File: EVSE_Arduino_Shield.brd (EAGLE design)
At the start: 68.6 x 53.3 mm, 45 parts, among them IC1 TLV1805DBVR, IC2 MT3608, IC3 TC1044S_OA, U2 ARDUINOR3-DIMENSION

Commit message: * Fixed missing values of R2, R3, C5, C1, C6, C4
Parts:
- C1, C4, C5, C6: value (none) -> 10u
- R2: value (none) -> 39k
- R3: value (none) -> 2k
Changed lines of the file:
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@@
 <drawing>
 <settings>
-<setting alwaysvectorfont="yes"/>
+<setting alwaysvectorfont="no"/>
 <setting verticaltext="up"/>
 </settings>
@@
 </autorouter>
 <elements>
-<element name="C1" library="rcl" library_urn="urn:adsk.eagle:library:334" package="C0805" package3d_urn="urn:adsk.eagle:package:23617/2" value="" x="26.5" y="25" smashed="yes">
+<element name="C1" library="rcl" library_urn="urn:adsk.eagle:library:334" package="C0805" package3d_urn="urn:adsk.eagle:package:23617/2" value="10u" x="26.5" y="25" smashed="yes">
 <attribute name="NAME" x="26.5" y="23.5" size="1" layer="25" font="vector" ratio="13" align="center"/>
 <attribute name="POPULARITY" value="88" x="41.74" y="3.41" size="1.778" layer="27" display="off"/>
@@
 <attribute name="VALUE" x="37.095" y="23.635" size="1.27" layer="27" rot="R270"/>
 </element>
-<element name="C4" library="rcl" library_urn="urn:adsk.eagle:library:334" package="C0805" package3d_urn="urn:adsk.eagle:package:23617/2" value="" x="30" y="30.5" smashed="yes" rot="R90">
+<element name="C4" library="rcl" library_urn="urn:adsk.eagle:library:334" package="C0805" package3d_urn="urn:adsk.eagle:package:23617/2" value="10u" x="30" y="30.5" smashed="yes" rot="R90">
 <attribute name="NAME" x="30" y="33.5" size="1" layer="25" font="vector" ratio="13" rot="R90" align="center"/>
 <attribute name="POPULARITY" value="88" x="51.59" y="50.82" size="1.778" layer="27" rot="R90" display="off"/>
@@
 <attribute name="VALUE" x="27.2" y="40.6" size="1.27" layer="27" rot="R270"/>
 </element>
-<element name="R2" library="rcl" library_urn="urn:adsk.eagle:library:334" package="R0603" package3d_urn="urn:adsk.eagle:package:23555/3" value="" x="29.5" y="43" smashed="yes" rot="R270">
+<element name="R2" library="rcl" library_urn="urn:adsk.eagle:library:334" package="R0603" package3d_urn="urn:adsk.eagle:package:23555/3" value="39k" x="29.5" y="43" smashed="yes" rot="R270">
 <attribute name="NAME" x="31" y="43" size="1" layer="25" font="vector" ratio="13" rot="R270" align="center"/>
 <attribute name="POPULARITY" value="70" x="29.5" y="43" size="1.27" layer="27" rot="R270" display="off"/>
@@
 <attribute name="VALUE" x="27.595" y="43.635" size="1.27" layer="27" rot="R270"/>
 </element>
-<element name="R3" library="rcl" library_urn="urn:adsk.eagle:library:334" package="R0603" package3d_urn="urn:adsk.eagle:package:23555/3" value="" x="26.5" y="45" smashed="yes">
+<element name="R3" library="rcl" library_urn="urn:adsk.eagle:library:334" package="R0603" package3d_urn="urn:adsk.eagle:package:23555/3" value="2k" x="26.5" y="45" smashed="yes">
 <attribute name="NAME" x="26.5" y="46.5" size="1" layer="25" font="vector" ratio="13" align="center"/>
 <attribute name="POPULARITY" value="70" x="26.5" y="45" size="1.27" layer="27" display="off"/>
@@
 <attribute name="VALUE" x="25.865" y="43.095" size="1.27" layer="27"/>
 </element>
-<element name="C5" library="rcl" library_urn="urn:adsk.eagle:library:334" package="C0805" package3d_urn="urn:adsk.eagle:package:23617/2" value="" x="23.5" y="44" smashed="yes" rot="R90">
+<element name="C5" library="rcl" library_urn="urn:adsk.eagle:library:334" package="C0805" package3d_urn="urn:adsk.eagle:package:23617/2" value="10u" x="23.5" y="44" smashed="yes" rot="R90">
 <attribute name="NAME" x="21.5" y="44" size="1" layer="25" font="vector" ratio="13" rot="R90" align="center"/>
 <attribute name="POPULARITY" value="88" x="23.5" y="44" size="1.27" layer="27" rot="R90" display="off"/>
@@
 <attribute name="VALUE" x="26.04" y="42.73" size="1.27" layer="27" rot="R90"/>
 </element>
-<element name="C6" library="rcl" library_urn="urn:adsk.eagle:library:334" package="C0805" package3d_urn="urn:adsk.eagle:package:23617/2" value="" x="31.5" y="39.5" smashed="yes" rot="R270">
+<element name="C6" library="rcl" library_urn="urn:adsk.eagle:library:334" package="C0805" package3d_urn="urn:adsk.eagle:package:23617/2" value="10u" x="31.5" y="39.5" smashed="yes" rot="R270">
 <attribute name="NAME" x="31.5" y="36" size="1" layer="25" font="vector" ratio="13" rot="R270" align="center"/>
 <attribute name="POPULARITY" value="88" x="31.5" y="39.5" size="1.27" layer="27" rot="R270" display="off"/>

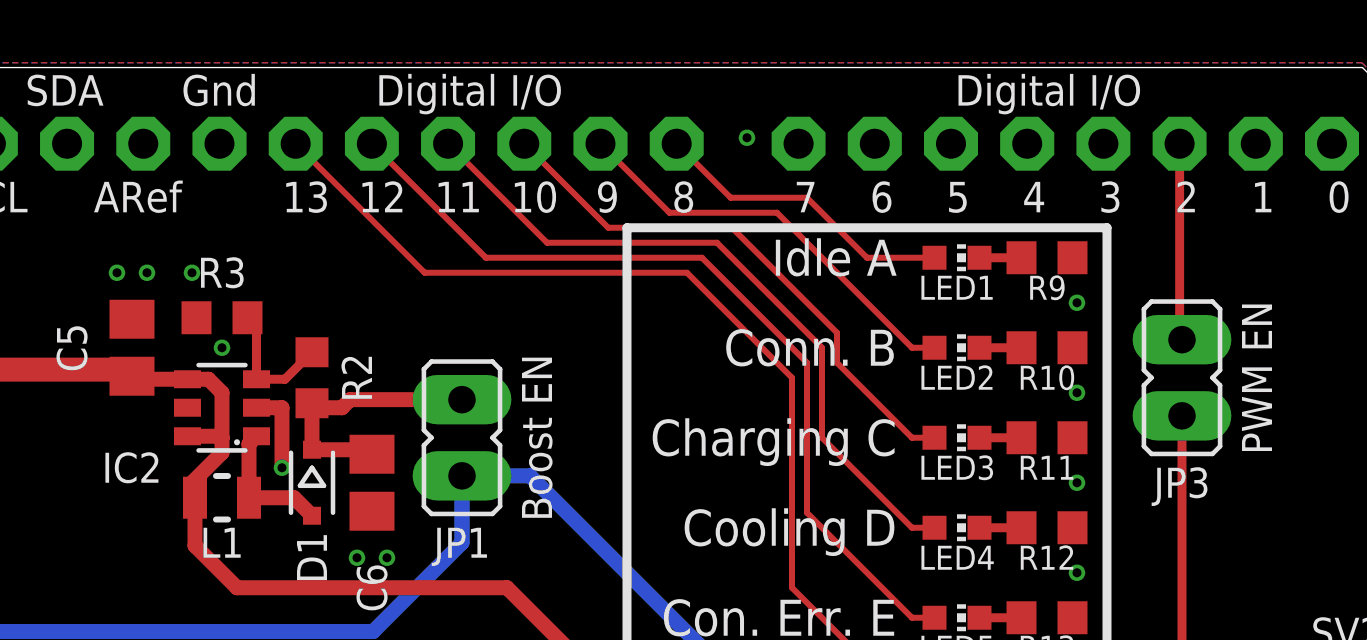
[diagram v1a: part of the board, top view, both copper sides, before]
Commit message: * Cleaned Code a bit * Fixed Issue #1 - PWM is now on D3 * Fixed Issue #2 . MT3608 has the correct pin out now * Re-generated GERBER and SCH
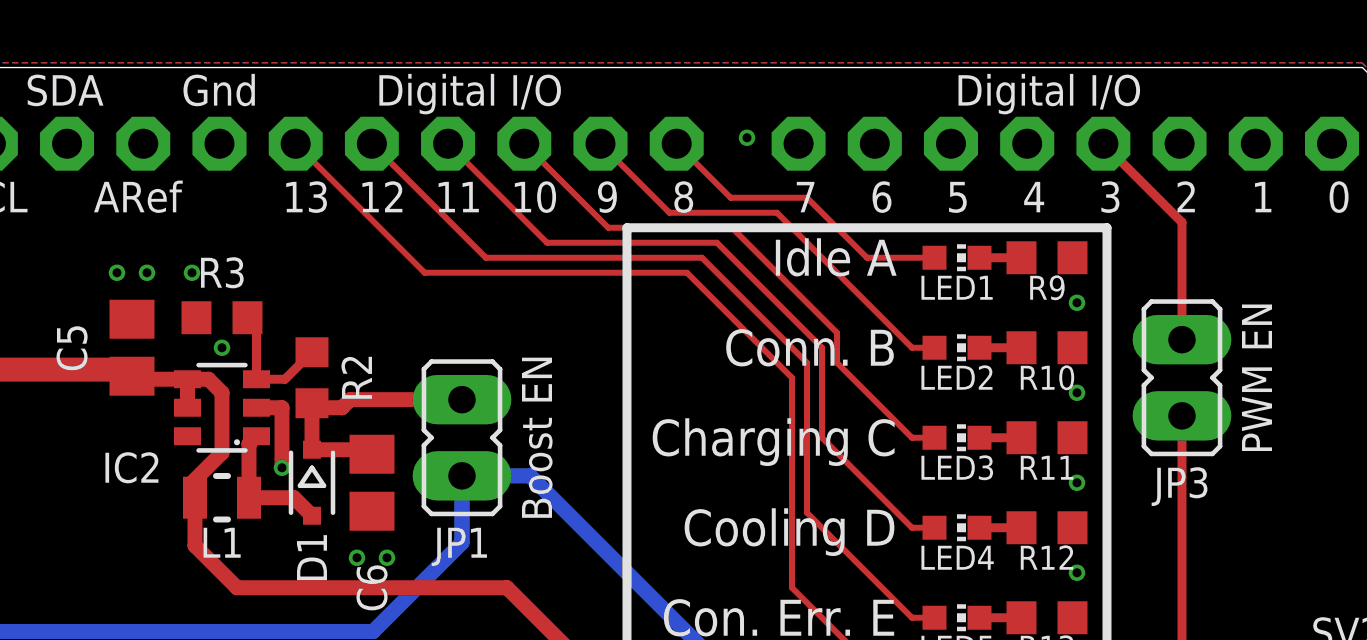
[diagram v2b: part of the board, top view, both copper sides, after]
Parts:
- J1: value (none) -> 691214310003
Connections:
- net +5V: now also IC2.5; no longer IC2.6
- net N$5: now also U2.D3; no longer U2.D2
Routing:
- net N$5: track 6.56 -> 7.73 mm
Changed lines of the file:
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@@
 <attribute name="VALUE" x="66.921" y="25.69" size="1.27" layer="27" ratio="10" rot="R90"/>
 </element>
-<element name="J1" library="Wurth_Connectors_WR-TBL Rising Cage Clamp" library_urn="urn:adsk.eagle:library:16280519" package="691214310003" package3d_urn="urn:adsk.eagle:package:16248452/2" value="" x="64" y="17.5" smashed="yes" rot="R90">
-<attribute name="DATASHEET-URL" value="https://www.we-online.com/catalog/datasheet/691214310003.pdf" x="64" y="17.5" size="1.27" layer="27" rot="R90" display="off"/>
+<element name="J1" library="Wurth_Connectors_WR-TBL Rising Cage Clamp" library_urn="urn:adsk.eagle:library:16280519" package="691214310003" package3d_urn="urn:adsk.eagle:package:16248452/2" value="691214310003" x="64" y="17.5" smashed="yes" rot="R90">
+<attribute name="DATASHEET-URL" value="https://www.we-online.com/redexpert/spec/691214310003?ae" x="64" y="17.5" size="1.27" layer="27" rot="R90" display="off"/>
 <attribute name="IR-UL" value="10A" x="64" y="17.5" size="1.27" layer="27" rot="R90" display="off"/>
 <attribute name="MOUNT" value="THT" x="64" y="17.5" size="1.27" layer="27" rot="R90" display="off"/>
@@
 </signal>
 <signal name="+5V">
-<contactref element="IC2" pad="6"/>
+<contactref element="IC2" pad="5"/>
 <contactref element="IC2" pad="4"/>
 <contactref element="C5" pad="1"/>
@@
 <wire x1="25.5" y1="39.5" x2="25.5" y2="39.1" width="0.5" layer="1"/>
 <wire x1="25.5" y1="39.1" x2="25.6" y2="39" width="0.5" layer="1"/>
-<wire x1="26.5" y1="42.5" x2="26.5" y2="41" width="0.5" layer="1"/>
-<wire x1="26.5" y1="41" x2="26.5" y2="40.5" width="0.5" layer="1"/>
-<wire x1="25.35" y1="41.05" x2="26.45" y2="41.05" width="0.5" layer="1"/>
-<wire x1="26.45" y1="41.05" x2="26.5" y2="41" width="0.5" layer="1"/>
+<wire x1="26.5" y1="42.5" x2="26.5" y2="40.5" width="0.5" layer="1"/>
 <wire x1="25.6" y1="39" x2="25.6" y2="37.4" width="0.5" layer="1"/>
 <wire x1="25.6" y1="37.4" x2="27" y2="36" width="0.5" layer="1"/>
@@
 <wire x1="42.5" y1="11" x2="42.5" y2="6.94" width="0.3" layer="16"/>
 <wire x1="42.5" y1="6.94" x2="38.1" y2="2.54" width="0.3" layer="16"/>
+<wire x1="25.35" y1="42" x2="25.35" y2="42.95" width="0.5" layer="1"/>
 </signal>
 <signal name="PWM_IN">
@@
 </signal>
 <signal name="N$5">
-<contactref element="U2" pad="D2"/>
 <contactref element="JP3" pad="2"/>
 <wire x1="58.5" y1="44.27" x2="58.42" y2="44.35" width="0.3" layer="1"/>
-<wire x1="58.42" y1="44.35" x2="58.42" y2="50.8" width="0.3" layer="1"/>
+<contactref element="U2" pad="D3"/>
+<wire x1="58.5" y1="44.27" x2="58.5" y2="48.18" width="0.3" layer="1"/>
+<wire x1="58.5" y1="48.18" x2="55.88" y2="50.8" width="0.3" layer="1"/>
 </signal>
 </signals>
